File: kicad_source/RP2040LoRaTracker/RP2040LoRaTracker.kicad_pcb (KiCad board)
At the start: 2 copper layers, 30 x 88 mm, 45 parts, among them J1 USB_B_Micro, SW1 SW_Push, SW2 SW_Push, U1 RP2040, U2 Ai-Thinker-Ra-01, U3 NEO-M8N, U4 W25Q16JVSS, U5 24LC32, Y1 Crystal_GND24_Small

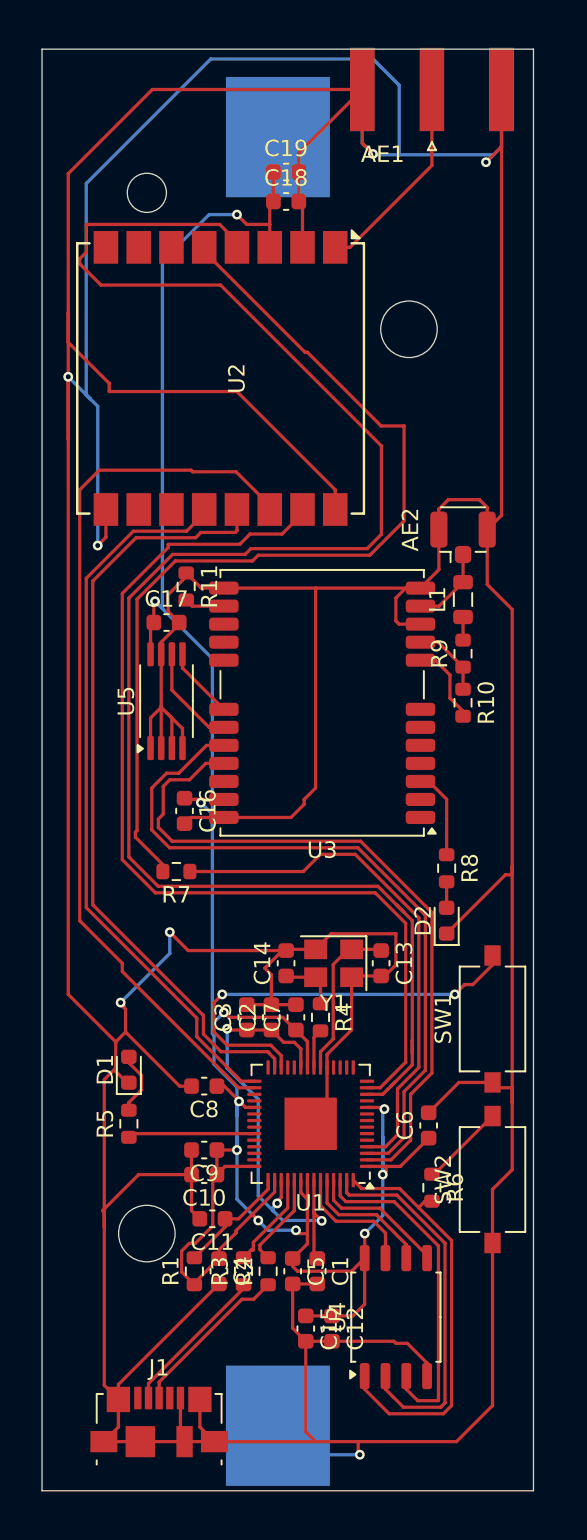
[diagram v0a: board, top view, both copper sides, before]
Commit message: added BME280 and quiic connector
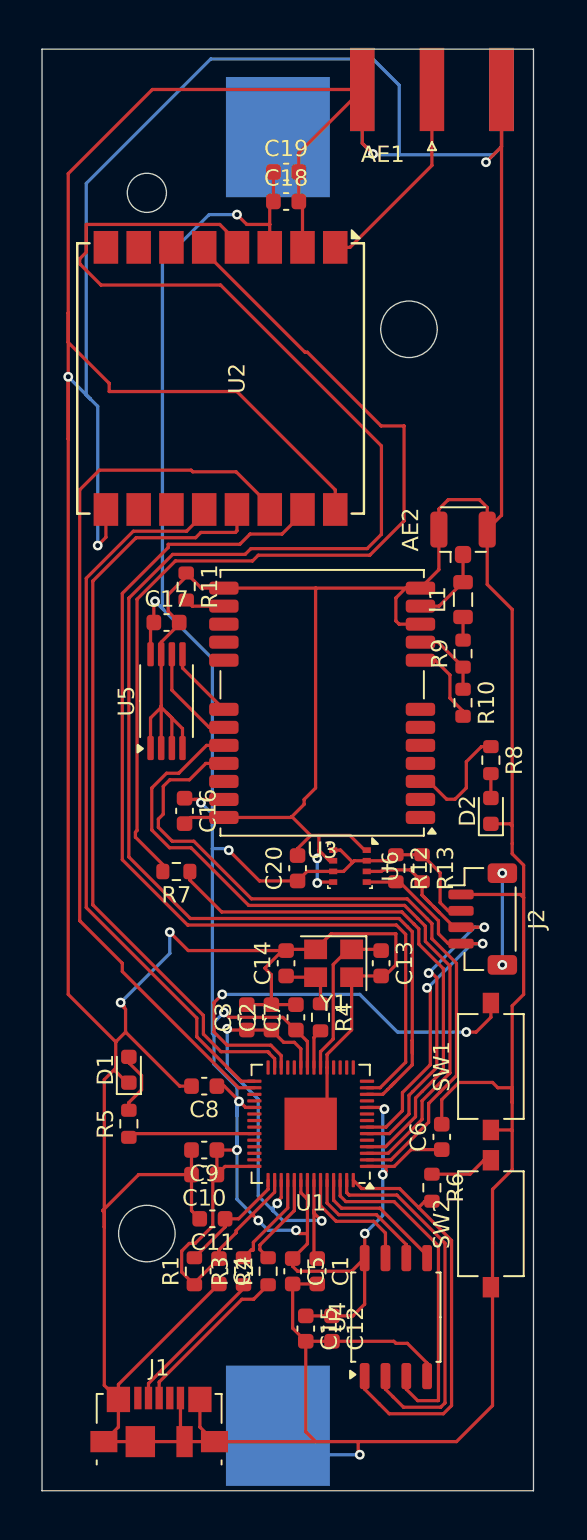
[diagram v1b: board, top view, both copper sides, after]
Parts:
- added C20: 100 nF, Capacitor_SMD:C_0603_1608Metric, F.Cu at (139.6, 104.0)
- added J2: BM04B-SRSS-TB, Connector_JST:JST_SH_BM04B-SRSS-TB_1x04-1MP_P1.00mm_Vertical, F.Cu at (150.9, 107.1)
- added R12: 10k, Resistor_SMD:R_0603_1608Metric, F.Cu at (145.6, 104.0)
- added R13: 10k, Resistor_SMD:R_0603_1608Metric, F.Cu at (147.2, 104.0)
- added U6: BME280, Package_LGA:Bosch_LGA-8_2.5x2.5mm_P0.65mm_ClockwisePinNumbering, F.Cu at (142.8, 103.9)
- moved D2 7.22 mm to (151.4, 100.5)
- moved R8 7.13 mm to (151.4, 97.4)
- moved SW1 2.90 mm to (151.4, 116.1)
- moved SW2 2.70 mm to (151.4, 125.7)
- moved C6 1.06 mm to (148.4, 120.4)
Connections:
- U1 pad 6: /RP2040/I2C_SDA -> I2C_SDA
- U1 pad 7: /RP2040/I2C_SCL -> I2C_SCL
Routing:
- net I2C_SDA: track 0.00 -> 27.5 mm, vias 0 -> 2
- net I2C_SCL: track 0.00 -> 24.5 mm, vias 0 -> 2
- net +3V3: track 158.1 -> 179.2 mm, vias 11 -> 12
- net GND: track 513.3 -> 526.9 mm, vias 7 -> 9
- net unconnected-(J2-MountPin-PadMP): track 0.00 -> 5.60 mm, vias 0 -> 2
- net /LoRa GNSS/TIMEPULSE: track 5.44 -> 7.02 mm
- net Net-(R6-Pad1): track 5.17 -> 3.95 mm
- net LORA_RESET: track 106.8 -> 105.8 mm
- net SERIAL_TX: track 43.4 -> 44.2 mm
- net SERIAL_RX: track 43.7 -> 44.5 mm
- net /RP2040/RUN: track 25.7 -> 26.5 mm

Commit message: added voltage regulator
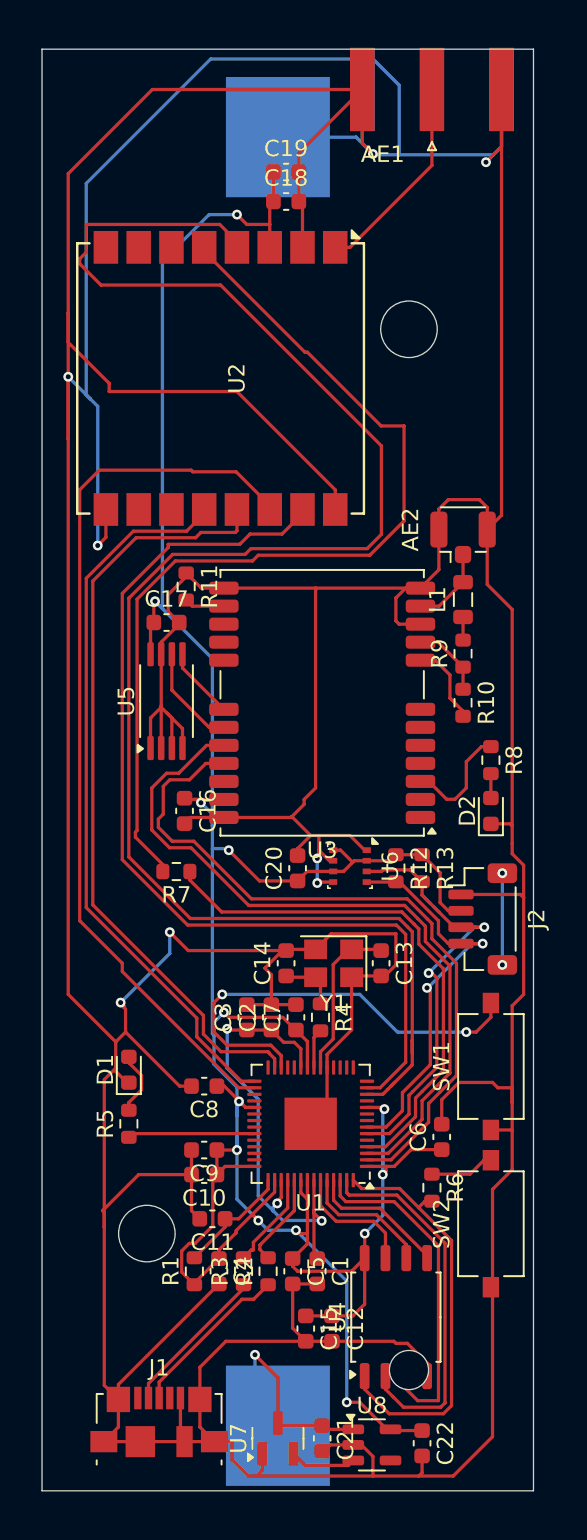
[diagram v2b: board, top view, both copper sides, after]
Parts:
- added C21: 2.2 uF, Capacitor_SMD:C_0603_1608Metric, F.Cu at (141.1, 138.8)
- added C22: 2.2 uF, Capacitor_SMD:C_0603_1608Metric, F.Cu at (147.2, 139.1)
- added U7: TPS3839DBZ, Package_TO_SOT_SMD:SOT-23, F.Cu at (138.4, 138.8)
- added U8: TPS73630DBV, Package_TO_SOT_SMD:SOT-23-5, F.Cu at (144.1, 139.2)
- turned BT1 to 90 degrees
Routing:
- net +3V3: track 179.2 -> 196.3 mm, vias 12 -> 13
- net +BATT: track 0.00 -> 16.9 mm, vias 0 -> 1
- net GND: track 526.9 -> 540.3 mm, vias 9 -> 8
- net Net-(U7-~{RESET}): track 0.00 -> 4.07 mm

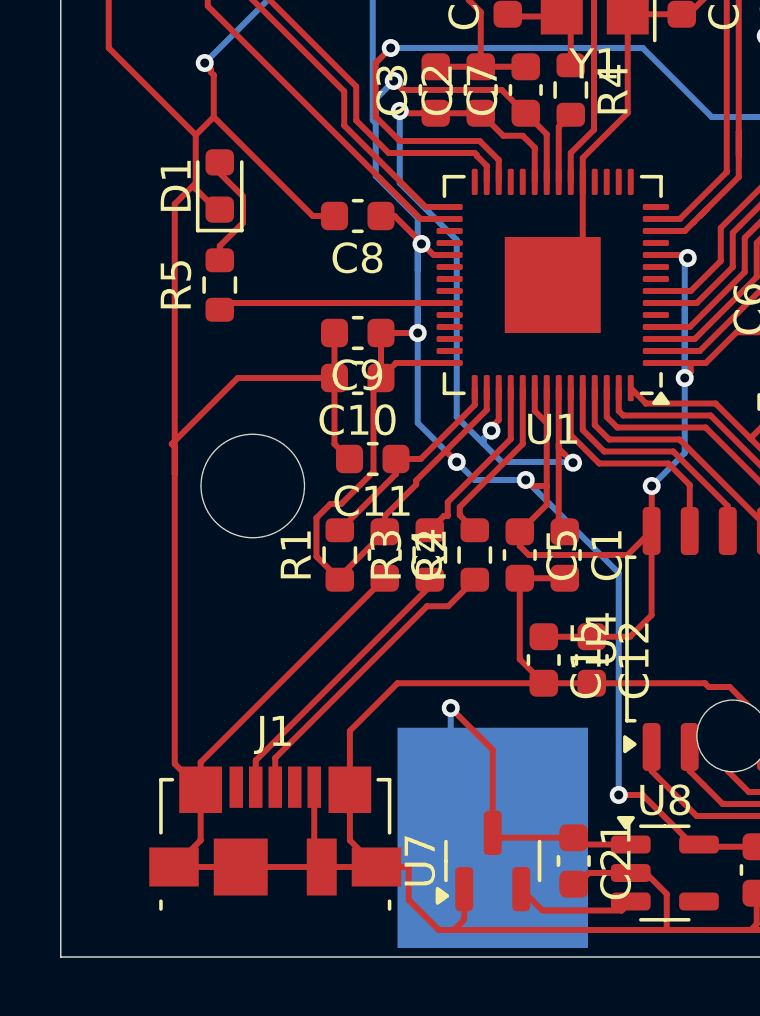
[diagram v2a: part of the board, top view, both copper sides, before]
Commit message: added battery charger
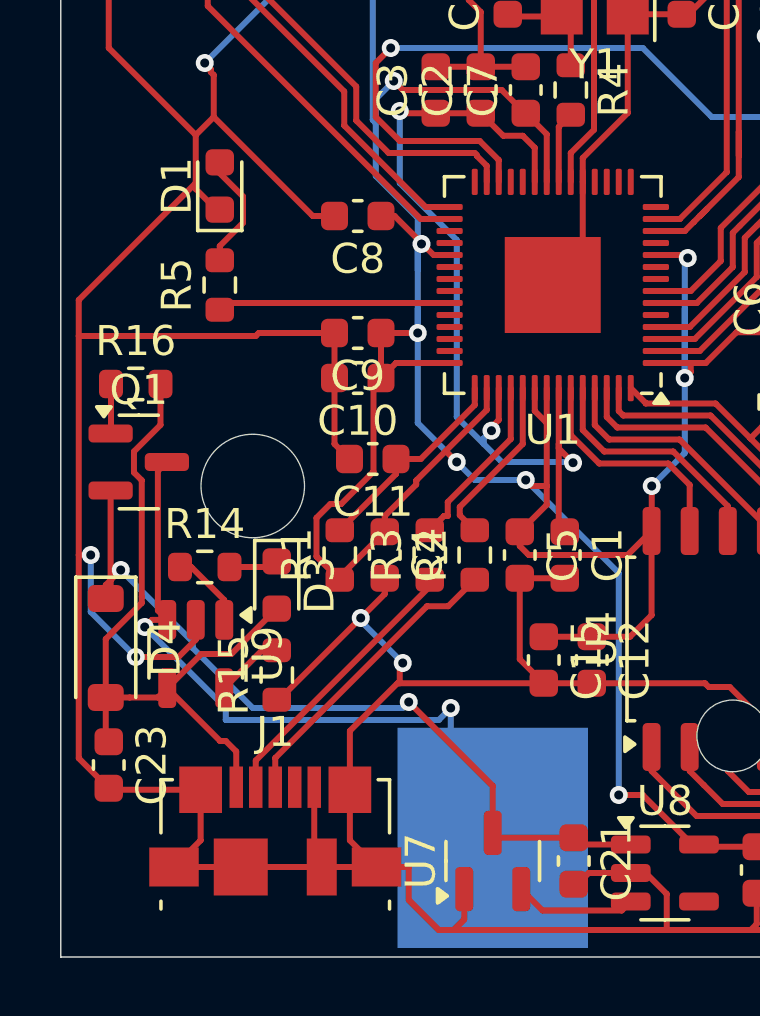
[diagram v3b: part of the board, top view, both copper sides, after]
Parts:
- added C23: 2.2 uF, Capacitor_SMD:C_0603_1608Metric, F.Cu at (125.6, 135.6)
- added D3: LED_Small, LED_SMD:LED_0603_1608Metric, F.Cu at (131.2, 129.6)
- added D4: MBR120, Diode_SMD:D_SOD-123, F.Cu at (125.5, 131.7)
- added Q1: NTR4171P, Package_TO_SOT_SMD:SOT-23, F.Cu at (126.6, 125.5)
- added R14: 4k7, Resistor_SMD:R_0603_1608Metric, F.Cu at (128.8, 129.0)
- added R15: 10k, Resistor_SMD:R_0603_1608Metric, F.Cu at (131.2, 132.6)
- added R16: 4k7, Resistor_SMD:R_0603_1608Metric, F.Cu at (126.5, 122.9)
- added U9: MCP73832-2-OT, Package_TO_SOT_SMD:SOT-23-5, F.Cu at (128.5, 131.9)
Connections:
- C21 pad 1: +BATT -> VCC
- J1 pad 1: unconnected-(J1-VBUS-Pad1) -> VBUS
- U7 pad 3: +BATT -> VCC
- U8 pad 1: +BATT -> VCC
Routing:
- net VCC: track 0.00 -> 26.8 mm, vias 0 -> 2
- net VBUS: track 0.00 -> 24.2 mm
- net GND: track 540.3 -> 552.0 mm, vias 8 -> 12
- net +BATT: track 16.9 -> 25.7 mm, vias 1 -> 2
- net Net-(U9-STAT): track 0.00 -> 2.59 mm
- net Net-(U9-PROG): track 0.00 -> 2.27 mm
- net Net-(Q1-G): track 0.00 -> 1.66 mm
- net Net-(D3-K): track 0.00 -> 1.65 mm

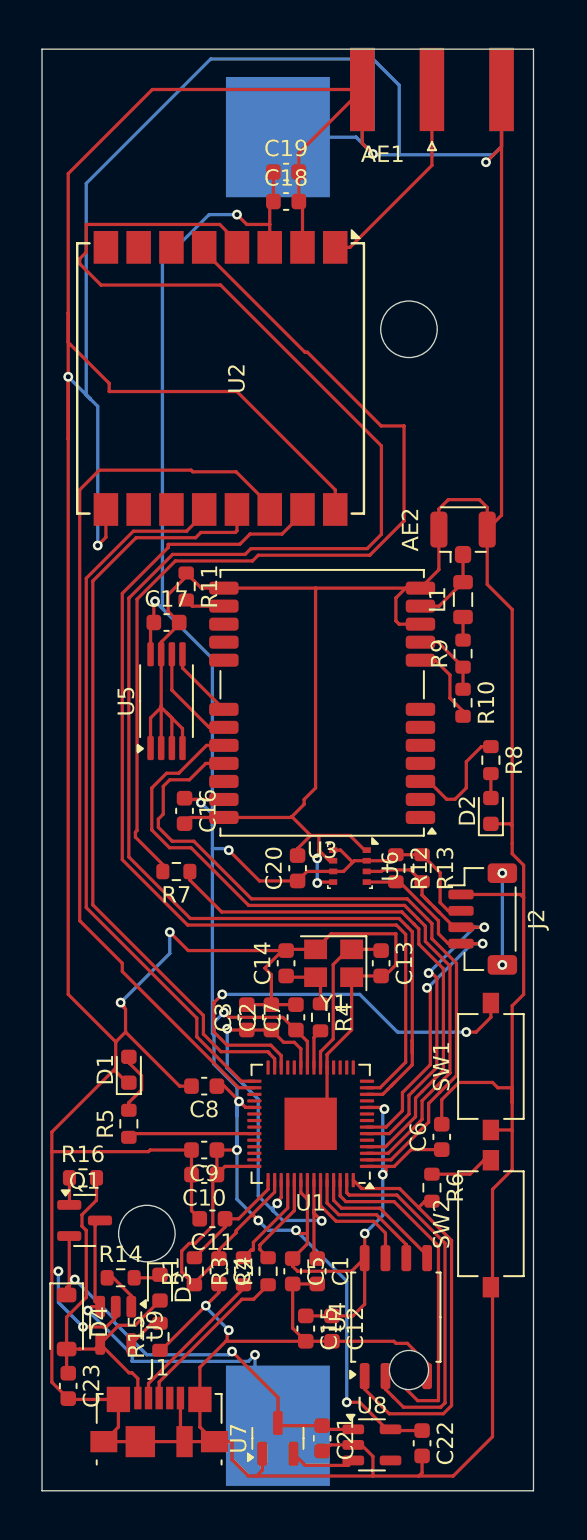
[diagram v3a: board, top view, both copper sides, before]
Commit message: changed battery holder, updated layout
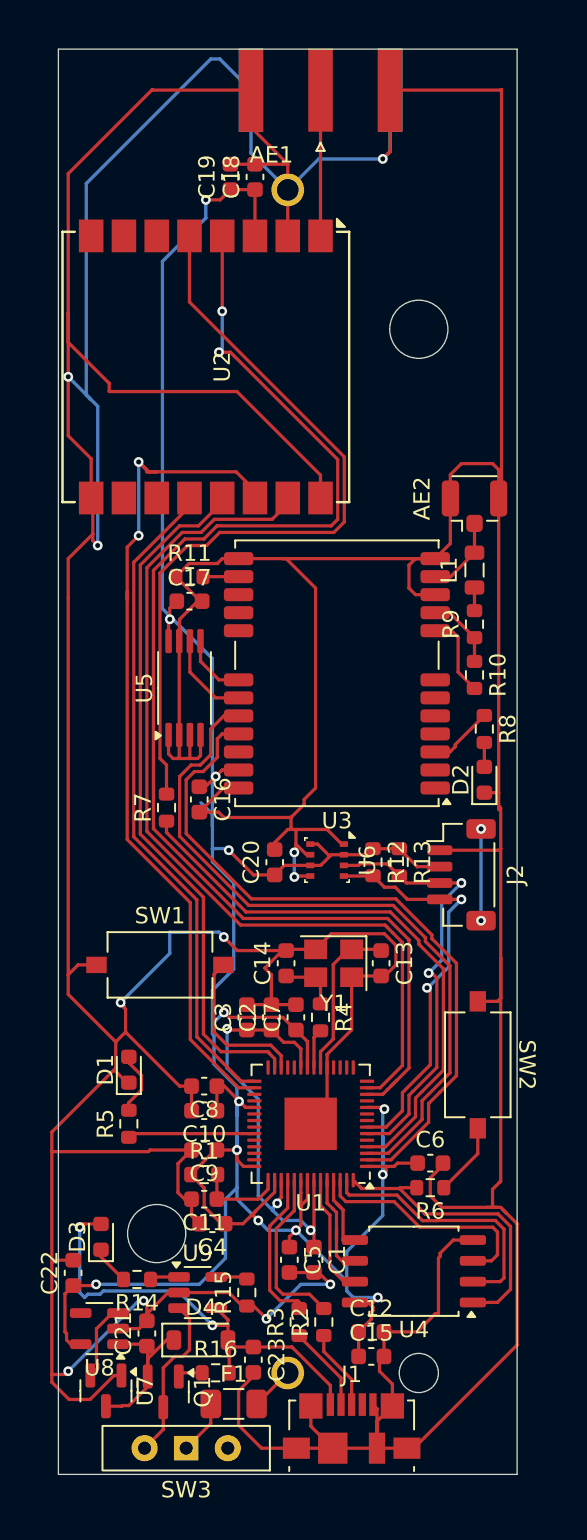
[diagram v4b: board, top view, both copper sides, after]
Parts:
- added F1: SF-1206S050, Fuse:Fuse_1206_3216Metric, F.Cu at (135.7, 136.7)
- added SW3: SW_SPDT, Button_Switch_THT:SW_Slide-03_Wuerth-WS-SLTV_10x2.5x6.4_P2.54mm, F.Cu at (132.8, 139.4)
- BT1: footprint Battery:BatteryHolder_Keystone_1042_1x18650 -> generationmake:KEYSTONE_1043
- moved C22 23.7 mm to (125.9, 128.7), turned to 90 degrees
- moved SW1 21.1 mm to (131.2, 109.9), turned to 0 degrees
- moved U8 18.1 mm to (127.5, 132.1), turned to 180 degrees
- moved R16 14.4 mm to (134.6, 134.8)
- moved C21 12.5 mm to (130.4, 132.4), turned to 90 degrees
- moved J1 11.8 mm to (142.9, 138.2)
- moved Q1 11.5 mm to (131.4, 136.0), turned to -90 degrees
- moved C23 11.4 mm to (136.9, 134.0)
- moved U7 10.9 mm to (127.9, 135.9), turned to -90 degrees
- moved SW2 9.73 mm to (150.6, 116.0), turned to -90 degrees
- moved D4 8.27 mm to (133.7, 132.8), turned to 0 degrees
- moved AE1 6.80 mm to (141.0, 56.5)
- moved R15 5.95 mm to (136.5, 129.9)
- moved R1 5.93 mm to (133.9, 122.7), turned to 0 degrees
- moved U9 5.39 mm to (133.5, 129.9), turned to 0 degrees
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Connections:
- BT1 pad 1: +BATT -> Net-(BT1-+)
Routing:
- net LORA_RESET: track 105.8 -> 79.2 mm, vias 0 -> 2
- net GND: track 552.0 -> 528.1 mm, vias 12 -> 11
- net /RP2040/RUN: track 26.5 -> 9.76 mm, vias 2 -> 0
- net VCC: track 26.8 -> 10.5 mm, vias 2 -> 0
- net +BATT: track 25.7 -> 10.2 mm, vias 2 -> 0
- net LORA_DIO0: track 58.3 -> 47.6 mm
- net +3V3: track 196.3 -> 186.8 mm
- net /RP2040/QSPI_SS: track 25.5 -> 18.3 mm
- net /RP2040/QSPI_SD1: track 22.8 -> 16.3 mm
- net /RP2040/QSPI_SD2: track 20.7 -> 14.5 mm
- net /RP2040/USB_DP: track 10.1 -> 4.92 mm
- net SPI_MISO: track 47.3 -> 42.6 mm
- net /RP2040/USB_DPX: track 5.81 -> 10.4 mm
- net LORA_CS: track 59.6 -> 55.3 mm
- net VBUS: track 24.2 -> 28.4 mm, vias 0 -> 2
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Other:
- board size 30 x 88 mm -> 28 x 87 mm

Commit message: beautified layout, made DRC
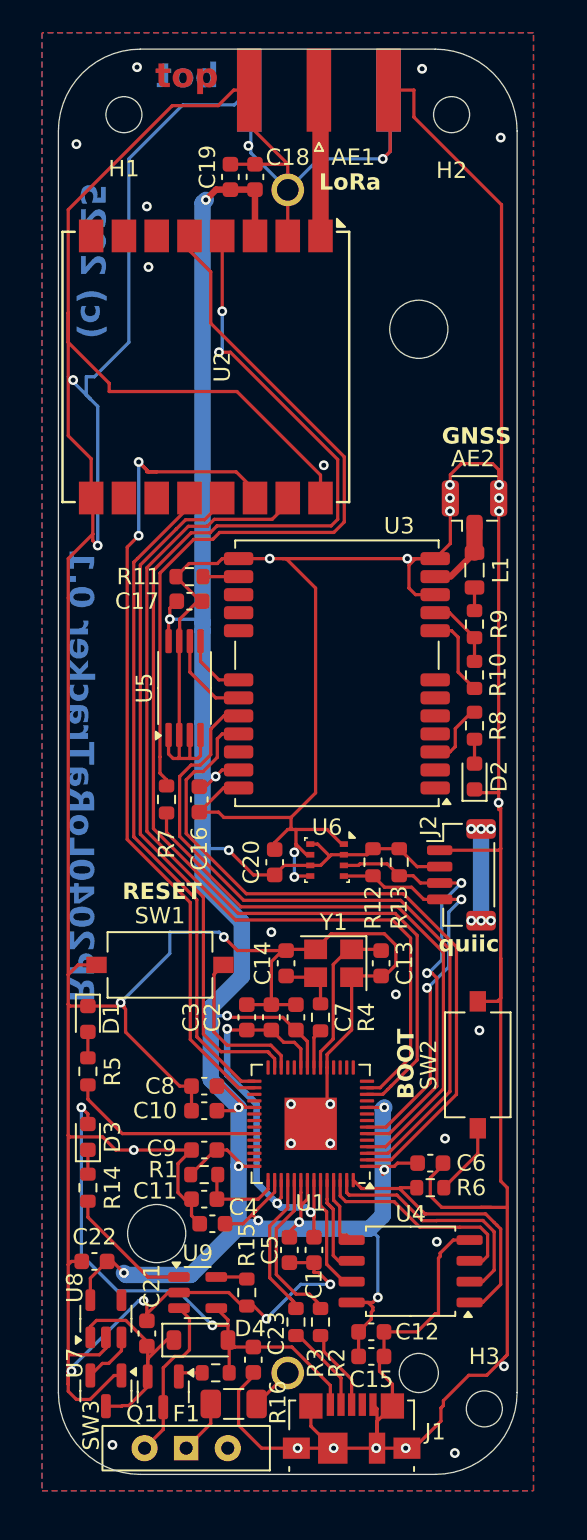
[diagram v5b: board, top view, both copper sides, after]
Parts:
- added FID1: Fiducial, generationmake:generationmake_small_solder, F.Cu at (153.4, 69.5)
- added FID2: Fiducial, generationmake:generationmake_logo, B.Cu at (144.2, 83.6)
- added H1: MountingHole, MountingHole:MountingHole_2.2mm_M2, F.Cu at (129.0, 58.0)
- added H2: MountingHole, MountingHole:MountingHole_2.2mm_M2, F.Cu at (149.0, 58.0)
- added H3: MountingHole, MountingHole:MountingHole_2.2mm_M2, F.Cu at (151.0, 137.0)
- moved R14 6.35 mm to (126.8, 123.5), turned to 90 degrees
- moved D3 6.15 mm to (126.8, 120.4)
- moved R5 4.06 mm to (126.8, 116.4)
- moved D1 3.98 mm to (126.8, 113.2), turned to -90 degrees
- moved C22 1.48 mm to (127.2, 128.0), turned to 180 degrees
- moved U8 0.72 mm to (127.9, 131.5), turned to 90 degrees
- moved R8 0.63 mm to (150.4, 95.3)
- moved D2 0.63 mm to (150.4, 98.4)
- moved C1 0.60 mm to (140.6, 127.3)
- moved C5 0.60 mm to (139.1, 127.3)
- moved R7 0.50 mm to (131.6, 99.8)
- moved R2 0.20 mm to (141.0, 131.7)
- moved R3 0.20 mm to (139.5, 131.7)
- moved U4 0.20 mm to (146.5, 128.6)
- moved AE1 0.10 mm to (140.9, 56.5)
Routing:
- net +3V3: track 186.8 -> 171.1 mm
- net GND: track 528.1 -> 520.0 mm, vias 11 -> 45
- net Net-(U9-STAT): track 1.80 -> 8.05 mm
- net VBUS: track 28.4 -> 33.8 mm
- net /RP2040/GPIO25: track 7.76 -> 11.9 mm
- net VCC: track 10.5 -> 14.0 mm
- net /RP2040/D1_R: track 3.90 -> 1.59 mm
- net /RP2040/QSPI_SD1: track 16.3 -> 14.7 mm
- net /RP2040/QSPI_SS: track 18.3 -> 16.9 mm
- net +1V1: track 27.6 -> 26.1 mm
- net Net-(U7-~{RESET}): track 4.78 -> 3.34 mm
- net /RP2040/QSPI_SD2: track 14.5 -> 13.5 mm
- net /RP2040/LORA_DIO0_R: track 34.6 -> 35.6 mm
- net Net-(D3-K): track 2.38 -> 1.49 mm
- net LORA_CS: track 55.3 -> 56.2 mm
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- added copper zone on B.Cu, net GND
- added copper zone on F.Cu, net GND
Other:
- outline, holes or cut-outs redrawn
- board text added: "(c) 2025"
- board text added: "BOOT"
- board text added: "GNSS"
- board text added: "LoRa"
- board text added: "RESET"
- board text added: "RP2040LoRaTracker 0.1"
- board text added: "bot"
- board text added: "quiic"
- board text added: "top"
